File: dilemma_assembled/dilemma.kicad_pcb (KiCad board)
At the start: 2 copper layers, 134 x 95.1 mm, 121 parts, among them J1 USB_C_Receptacle_USB2.0, J102 Serial, J103 Serial, J105 Conn_01x04_Female, J107 Conn_01x08_Female, J108 Conn_01x01_Female, J109 Conn_01x01_Female, J113 Cirque, J5 Conn_01x02, SW1 SW_Push, SW101 SW_Push, SW102 SW_Push, SW103 SW_Push, SW104 SW_Push, SW105 SW_Push, SW106 SW_Push, SW107 SW_Push, SW108 SW_Push, SW109 SW_Push, SW110 SW_SPST, SW111 SW_SPST, SW112 SW_Push, SW113 SW_Push, SW114 SW_Push, SW115 SW_Push, SW116 SW_Push, SW117 SW_Push, SW118 SW_Push, SW119 locked, SW2 SW_Push, U1 RP2040, U2 GD25Q80CEIGR, U3 XC6210B332MR-G, Y1 Crystal_GND24

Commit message: silkscreen
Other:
- board text removed: "5V"
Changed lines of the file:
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@@
     (effects (font (size 0.7 0.7) (thickness 0.12)) (justify mirror))
   )
-  (gr_text "5V" (at 169.224993 80.532262 90) (layer "B.SilkS")
+  (gr_text "3V3" (at 169.22 80.95 90) (layer "B.SilkS")
     (effects (font (size 0.8 0.8) (thickness 0.15)) (justify mirror))
   )
@@
     (effects (font (size 0.8 0.8) (thickness 0.12)))
   )
-  (gr_text "5V" (at 169.224993 80.532262 90) (layer "F.SilkS")
+  (gr_text "3V3" (at 169.22 80.95 90) (layer "F.SilkS")
     (effects (font (size 0.8 0.8) (thickness 0.15)))
   )

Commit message: zones
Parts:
- turned R4 to 180 degrees
- turned R5 to 90 degrees
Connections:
- R4 pad 1: Net-(J1-PadA5) -> Gnd_l
- R4 pad 2: Gnd_l -> Net-(J1-PadA5)
- R5 pad 1: Net-(J1-PadB5) -> Gnd_l
- R5 pad 2: Gnd_l -> Net-(J1-PadB5)
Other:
- board text added: "a1.0e"
- board text removed: "a1.0d"

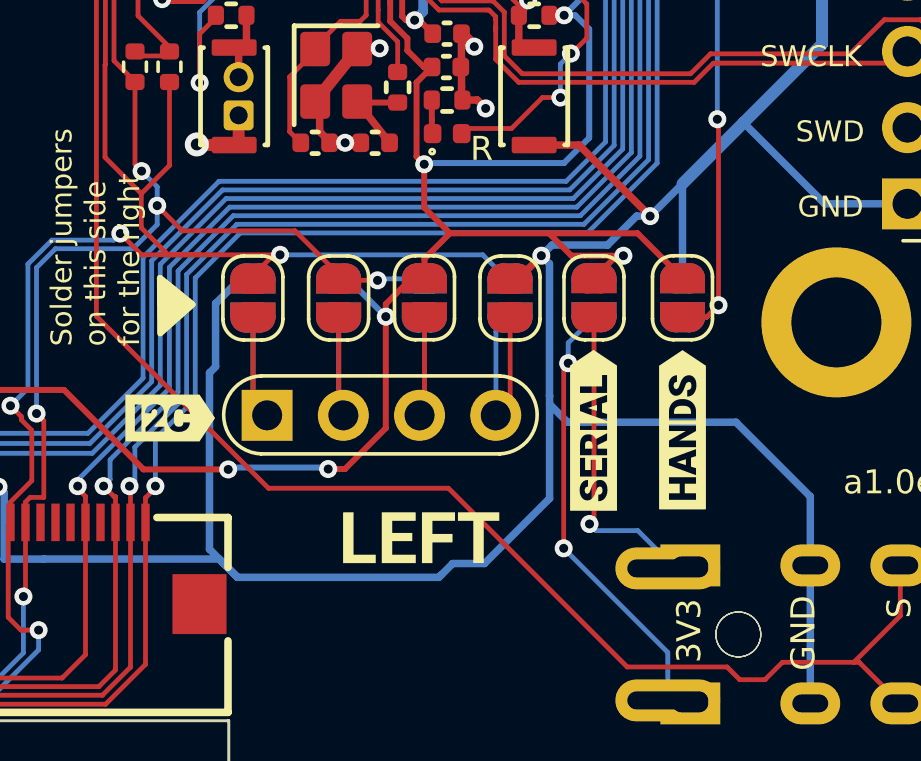
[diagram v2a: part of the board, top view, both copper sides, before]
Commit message: flip i2c
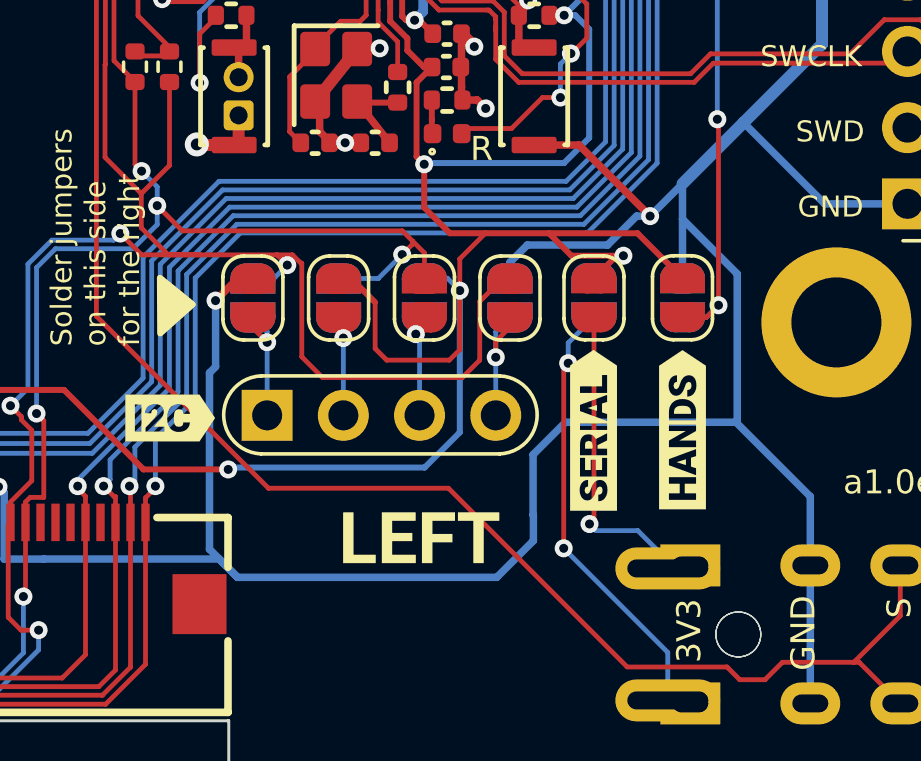
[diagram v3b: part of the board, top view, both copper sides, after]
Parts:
- JP103, JP105, JP107, JP109: moved to B.Cu
- JP104, JP106, JP108, JP110: moved to F.Cu
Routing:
- net +3V3: track 164.4 -> 173.5 mm, vias 8 -> 7
- net sda_l: track 74.4 -> 80.7 mm
- net scl_l: track 58.7 -> 62.2 mm
- net Gnd_l: track 199.8 -> 202.0 mm
- net Net-(JP105-Pad2): track 6.65 -> 4.53 mm, vias 0 -> 1
- net Net-(JP106-Pad2): track 6.65 -> 5.14 mm, vias 0 -> 1
- net Net-(JP104-Pad2): track 6.92 -> 5.65 mm, vias 0 -> 1
- net Net-(JP103-Pad2): track 6.92 -> 5.82 mm, vias 0 -> 1
